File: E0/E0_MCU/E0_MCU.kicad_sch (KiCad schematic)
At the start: 15 parts, among them J1 Conn_01x15, J2 Conn_01x15, J3 USB_OTG, U1 STM32F103C8T6, U2 Regulator_TBD, Y1 Crystal_TBD

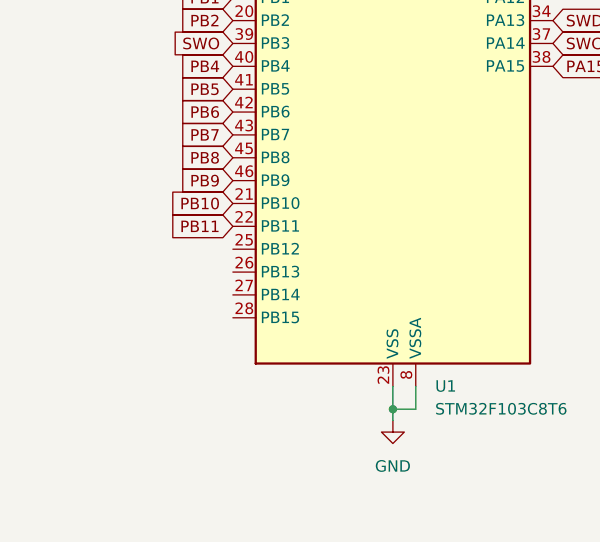
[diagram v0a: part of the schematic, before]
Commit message: fix: connect PB12-PB15 header nets
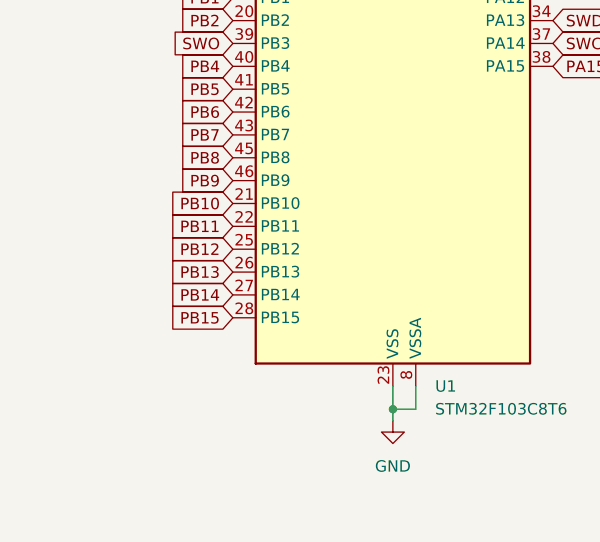
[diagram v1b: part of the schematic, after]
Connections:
- net PB12: now also U1.25 (PB12)
- net PB13: now also U1.26 (PB13)
- net PB14: now also U1.27 (PB14)
- net PB15: now also U1.28 (PB15)
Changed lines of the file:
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@@
+		)
+	)
+	(global_label "PB15"
+		(shape input)
+		(at 43.18 167.64 180)
+		(fields_autoplaced yes)
+		(effects
+			(font
+				(size 1.27 1.27)
+			)
+			(justify right)
+		)
+		(property "Intersheetrefs" "${INTERSHEET_REFS}"
+			(at 35.2358 167.64 0)
+			(effects
+				(font
+					(size 1.27 1.27)
+				)
+				(justify right)
+				(hide yes)
+			)
 		)
 	)
@@
 		)
 	)
+	(global_label "PB12"
+		(shape input)
+		(at 43.18 160.02 180)
+		(fields_autoplaced yes)
+		(effects
+			(font
+				(size 1.27 1.27)
+			)
+			(justify right)
+		)
+		(property "Intersheetrefs" "${INTERSHEET_REFS}"
+			(at 35.2358 160.02 0)
+			(effects
+				(font
+					(size 1.27 1.27)
+				)
+				(justify right)
+				(hide yes)
+			)
+		)
+	)
 	(global_label "PA5"
 		(shape input)
@@
 		)
 	)
+	(global_label "PB13"
+		(shape input)
+		(at 43.18 162.56 180)
+		(fields_autoplaced yes)
+		(effects
+			(font
+				(size 1.27 1.27)
+			)
+			(justify right)
+		)
+		(property "Intersheetrefs" "${INTERSHEET_REFS}"
+			(at 35.2358 162.56 0)
+			(effects
+				(font
+					(size 1.27 1.27)
+				)
+				(justify right)
+				(hide yes)
+			)
+		)
+	)
 	(global_label "PB11"
 		(shape input)
@@
 			(effects
 				(font
+					(size 1.27 1.27)
+				)
+				(justify right)
+				(hide yes)
+			)
+		)
+	)
+	(global_label "PB14"
+		(shape input)
+		(at 43.18 165.1 180)
+		(fields_autoplaced yes)
+		(effects
+			(font
+				(size 1.27 1.27)
+			)
+			(justify right)
+		)
+		(property "Intersheetrefs" "${INTERSHEET_REFS}"
+			(at 35.2358 165.1 0)
+			(effects
+				(font

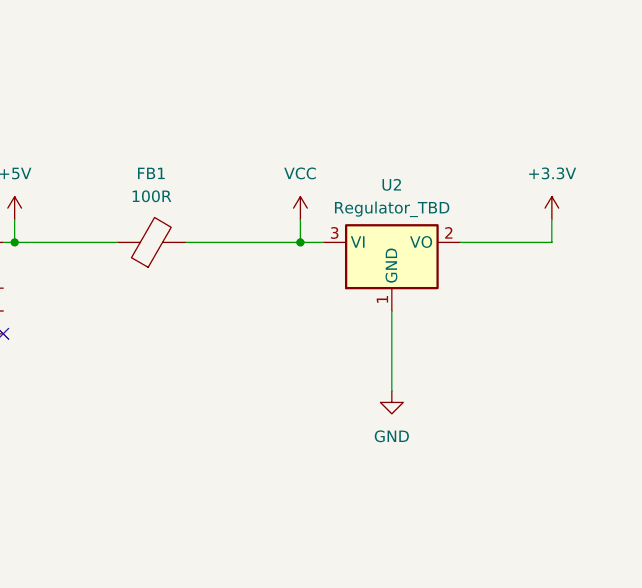
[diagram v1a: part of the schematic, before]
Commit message: feat: add AP2112 regulator and supply capacitors
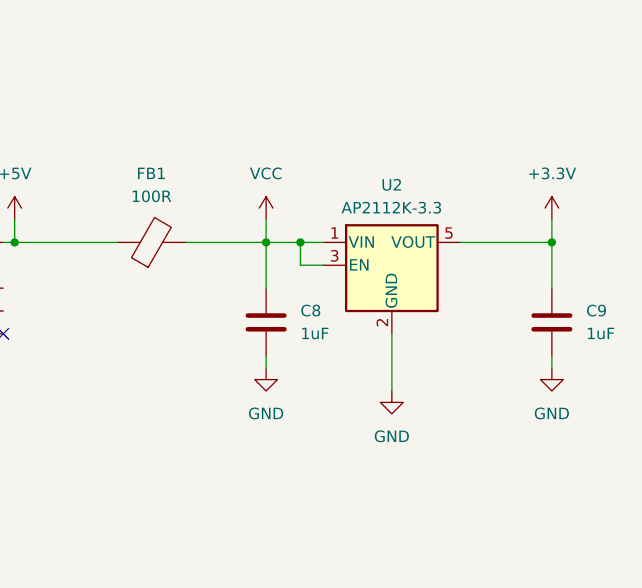
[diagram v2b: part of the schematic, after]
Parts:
- removed U2: Regulator_TBD, Package_TO_SOT_SMD:TO-252-3_TabPin2, symbol Regulator_Linear:LM1117DT-3.3
- added C8, C9: 1uF, symbol Device:C
- added U2: AP2112K-3.3, Package_TO_SOT_SMD:SOT-23-5, symbol Regulator_Linear:AP2112K-3.3
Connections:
- net +3.3V: now also C9.1, U2.5 (VOUT)
- net GND: now also C8.2, C9.2, U2.2 (GND)
- net VCC: now also C8.1, U2.1 (VIN), U2.3 (EN)

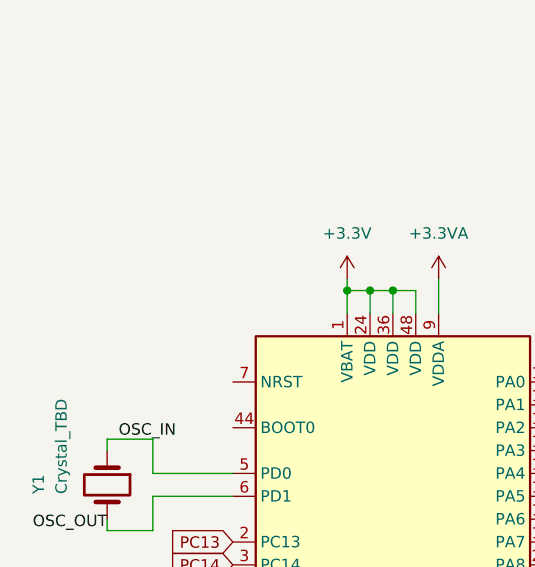
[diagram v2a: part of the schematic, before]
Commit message: feat: add NRST reset button
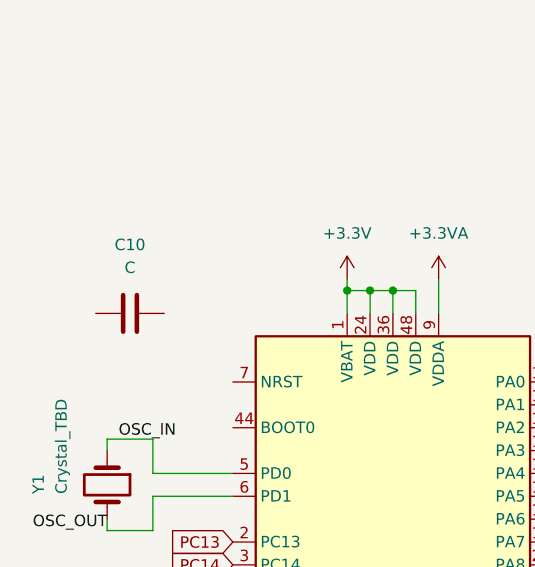
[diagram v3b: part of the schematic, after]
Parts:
- added C10: C, symbol Device:C
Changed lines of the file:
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@@
+	)
+	(symbol
+		(lib_id "Device:C")
+		(at 31.75 93.98 270)
+		(unit 1)
+		(exclude_from_sim no)
+		(in_bom yes)
+		(on_board yes)
+		(dnp no)
+		(fields_autoplaced yes)
+		(property "Reference" "C10"
+			(at 31.75 86.36 90)
+			(effects
+				(font
+					(size 1.27 1.27)
+				)
+			)
+		)
+		(property "Value" "C"
+			(at 31.75 88.9 90)
+			(effects
+				(font
+					(size 1.27 1.27)
+				)
+			)
+		)
+		(property "Footprint" ""
+			(at 27.94 94.9452 0)
+			(effects
+				(font
+					(size 1.27 1.27)
+				)
+				(hide yes)
+			)
+		)
+		(property "Datasheet" "~"
+			(at 31.75 93.98 0)
+			(effects
+				(font
+					(size 1.27 1.27)
+				)
+				(hide yes)
+			)
+		)
+		(property "Description" "Unpolarized capacitor"
+			(at 31.75 93.98 0)
+			(effects
+				(font
+					(size 1.27 1.27)
+				)
+				(hide yes)
+			)
+		)
+		(pin "2"
+		)
+		(pin "1"
+		)
+		(instances
+			(project ""
+				(path "/8f07bb29-36bc-46a4-8003-1764bbfc884c"
+					(reference "C10")
+					(unit 1)
+				)
+			)
+		)
 	)
 	(symbol

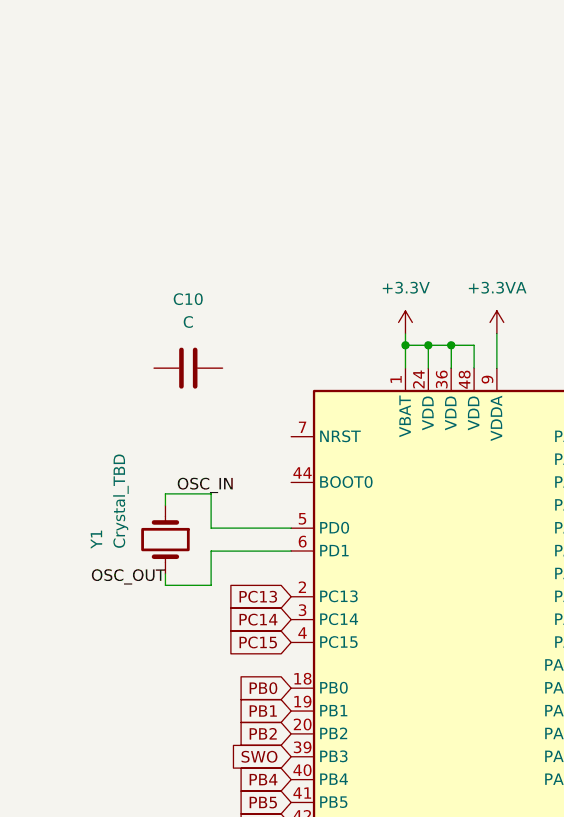
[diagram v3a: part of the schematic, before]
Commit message: feat: add BOOT0 pull-down resistor
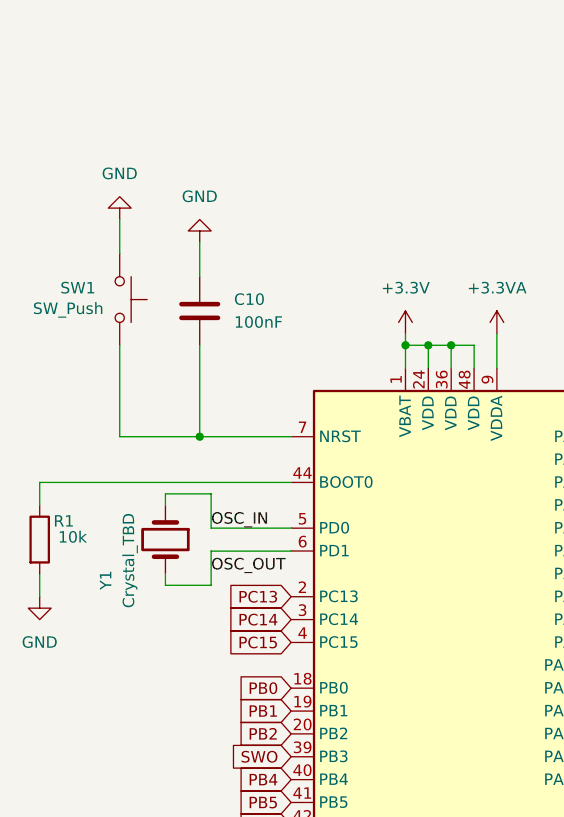
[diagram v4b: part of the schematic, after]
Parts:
- added R1: 10k, symbol Device:R
- added SW1: SW_Push, symbol Switch:SW_Push
- C10: value C -> 100nF
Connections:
- net GND: now also C10.2, R1.2, SW1.1
- net at C10.1: now also U1.7 (NRST), SW1.2
- net at U1.44 (BOOT0): now also R1.1
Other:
- moved on the sheet: C10

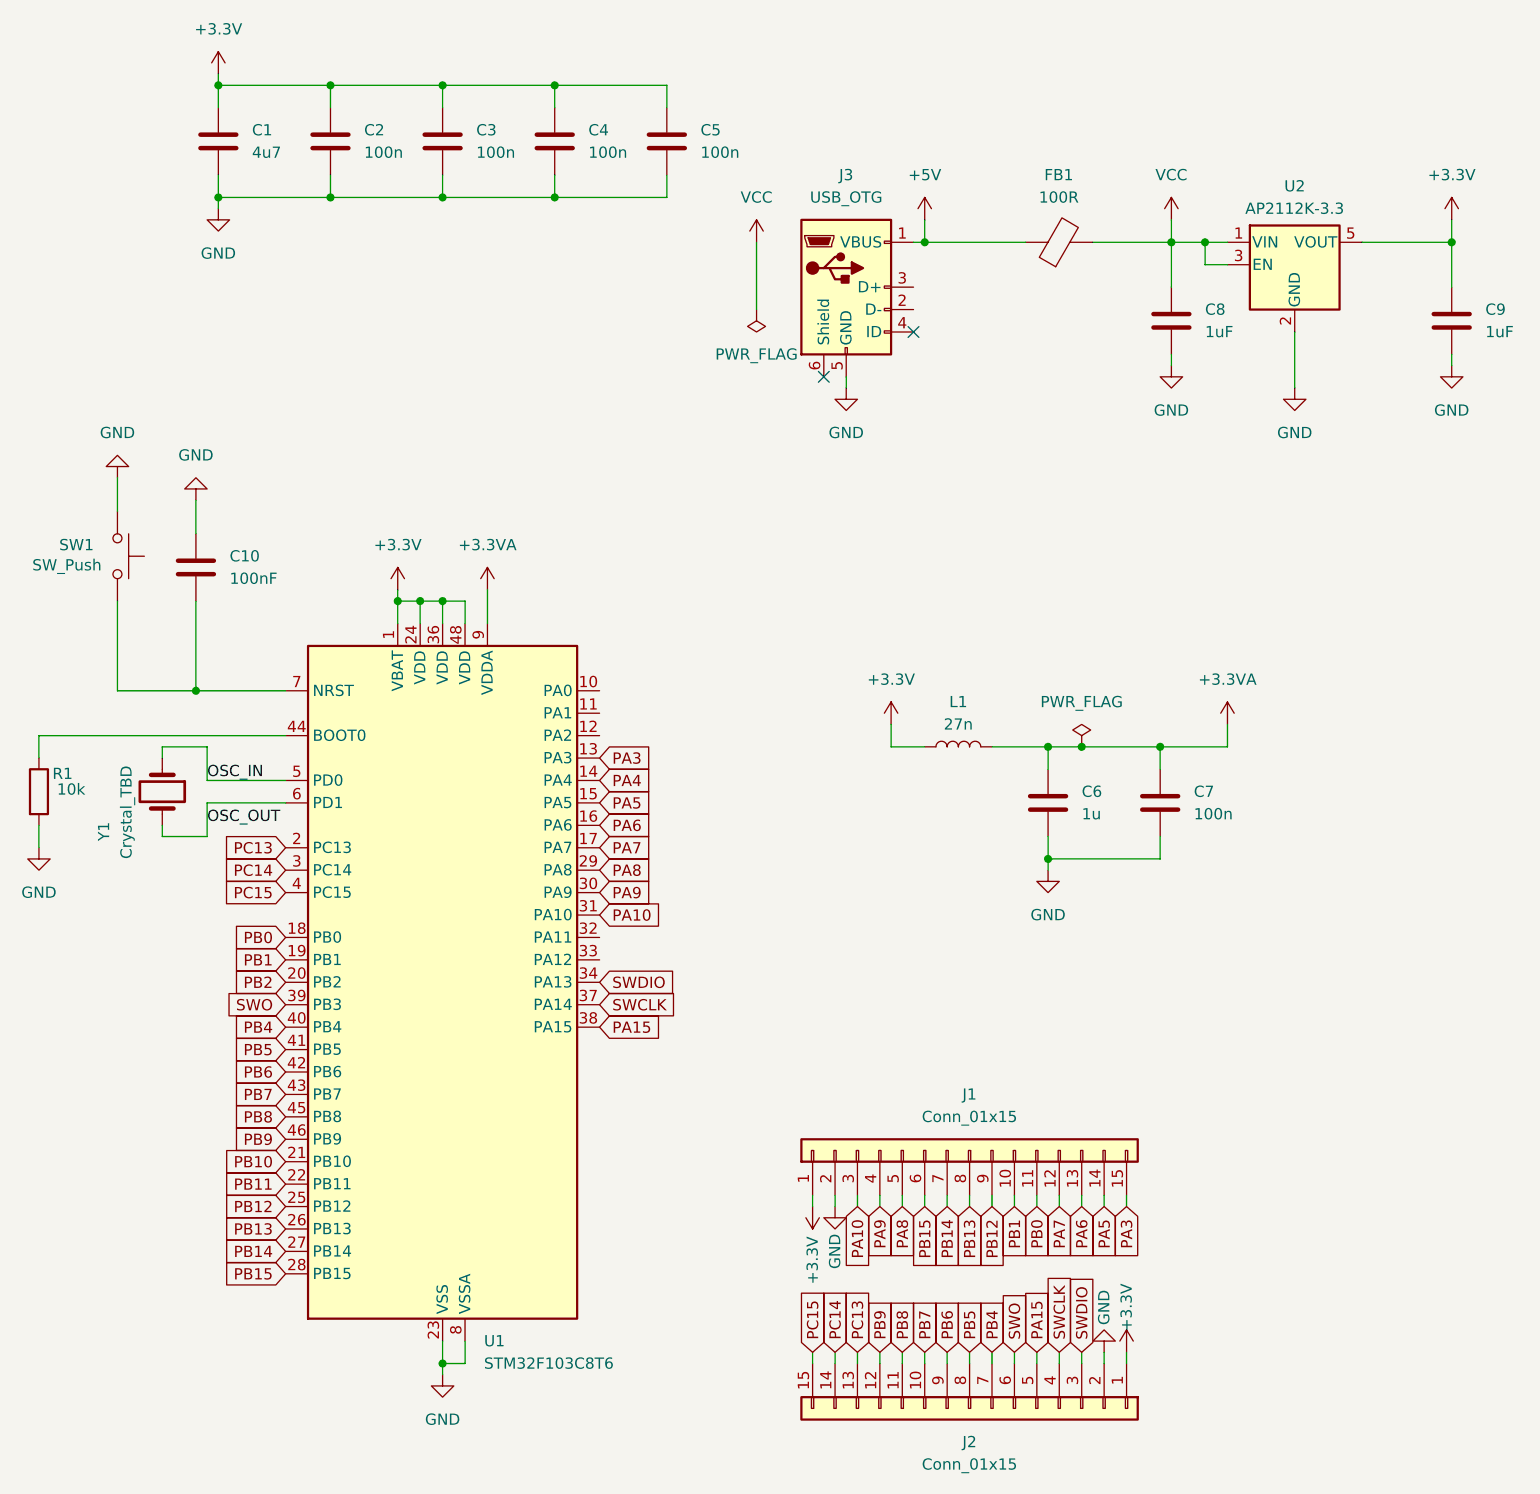
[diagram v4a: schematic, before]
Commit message: feat: complete E0 crystal circuit, ERC cleanup
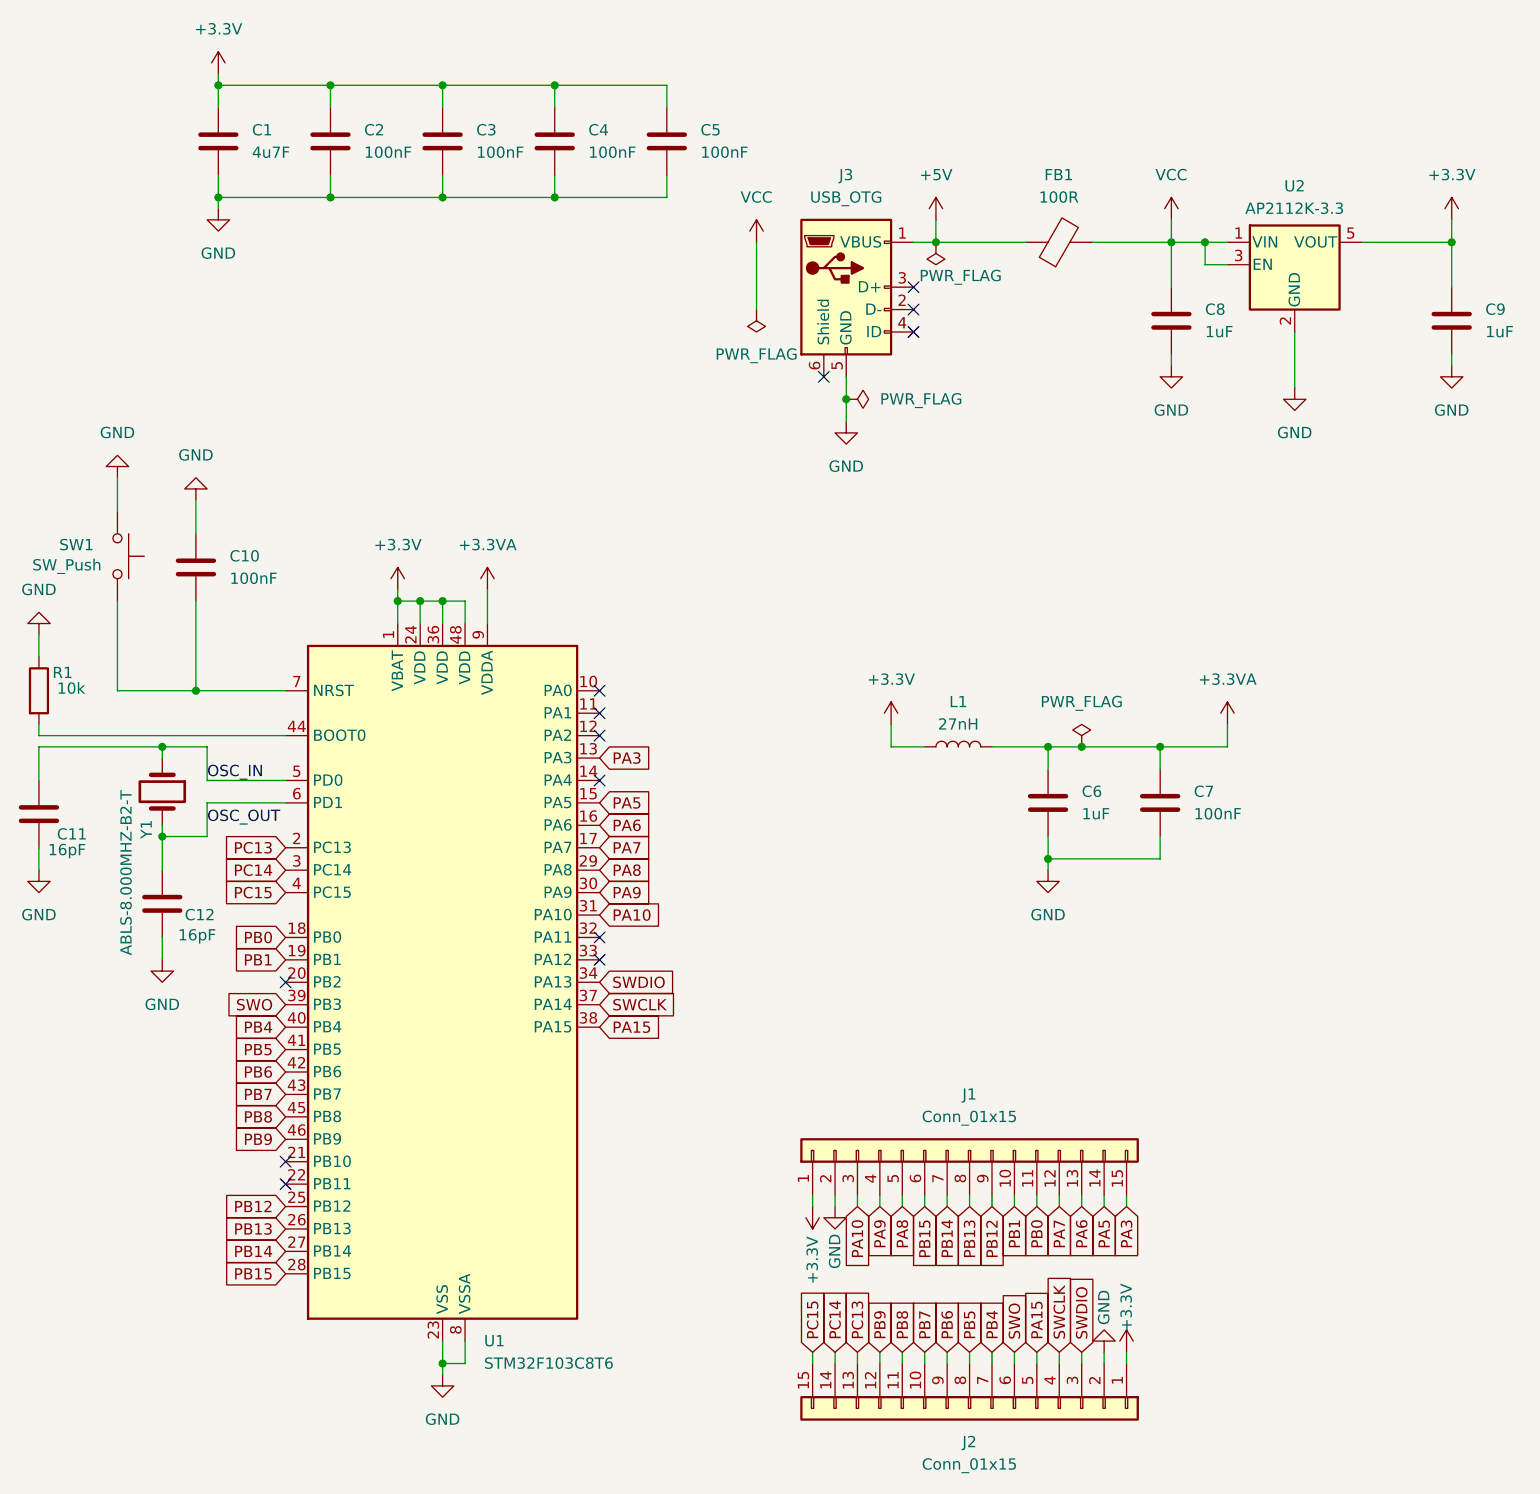
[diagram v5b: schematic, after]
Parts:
- added C11, C12: 16pF, symbol Device:C
- C1: value 4u7 -> 4u7F
- C2, C3, C4, C5, C7: value 100n -> 100nF
- C6: value 1u -> 1uF
- L1: value 27n -> 27nH
- Y1: value Crystal_TBD -> ABLS-8.000MHZ-B2-T
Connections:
- net GND: now also R1.1, C11.2, C12.2; no longer R1.2
- net OSC_IN: now also C11.1
- net OSC_OUT: now also C12.1
- net at U1.44 (BOOT0): now also R1.2; no longer R1.1
- net PA4: no longer names the net of U1.14 (PA4)
- net PB10: no longer names the net of U1.21 (PB10)
- net PB11: no longer names the net of U1.22 (PB11)
- net PB2: no longer names the net of U1.20 (PB2)
- no-connect marks 2 -> 13
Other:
- moved on the sheet: R1
